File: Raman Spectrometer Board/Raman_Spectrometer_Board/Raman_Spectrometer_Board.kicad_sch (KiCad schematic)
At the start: 33 parts, among them J1 RJ45_LED_Shielded, Q1 BSS138, Q2 BSS138, Q3 BSS138, Q4 BSS138, SW1 SW_Push, SW2 SW_Push, U1 Teensy4.1_DEV-16771, U2 OKI 12V-5V

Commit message: Rev 2 updated
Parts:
- added Conn10, Conn9: Molex_SL_02, MRDT_Connectors:MOLEX_SL_02_Vertical, symbol MRDT_Connectors:Molex_SL_02
- Conn7: footprint (none) -> MRDT_Connectors:MOLEX_SL_04_Vertical
- Conn8: footprint (none) -> MRDT_Connectors:MOLEX_SL_02_Vertical
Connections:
- net +3V3 is gone; now on net +3.3V: Conn8.1
- net +3.3V: now also Conn10.1, Conn9.1
- net CCD_Vout: now also U1.34 (RX8); no longer U1.26 (A12)
- net Encoder A: now also U1.22 (A8); no longer U1.37 (CS3)
- net Encoder B: now also U1.23 (A9); no longer U1.36 (CS2)
- net Green_Laser_3.3V: now also U1.33 (MCLK2); no longer U1.23 (A9)
- net Limit Switch 1: now also U1.30 (CRX3)
- net SW1: now also U1.40 (A16); no longer U1.41 (A17)
- net SW2: now also U1.41 (A17); no longer U1.40 (A16)
- net Limit Switch 3: now reaches U1.28 (RX7)
- net Limit Switch 3: now also Conn10.2
- net Limit Switch 2: now reaches U1.29 (TX7)
- net Limit Switch 2: now also Conn9.2
- net Diode Control: no longer names the net of U1.2 (OUT2)
- net Green_LED: no longer names the net of U1.1 (TX1)
- net Red_LED: no longer names the net of U1.0 (RX1)
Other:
- note added: "Limit Switches"
- note added: "Motor Encoder"
- note removed: "Limit Switch"
- note removed: "Motor encoder"
- moved on the sheet: Conn8, U1

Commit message: updated Raman PCB
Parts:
- added Conn11: GimbalA, MRDT_Connectors:MOLEX_SL_03_Vertical, symbol MRDT_Connectors:Molex_SL_03
- added Conn12: GimbalB, MRDT_Connectors:MOLEX_SL_03_Vertical, symbol MRDT_Connectors:Molex_SL_03
- Conn10: value Molex_SL_02 -> LimitSwitch3
- Conn7: value Molex_SL_04 -> MotorEncoder
- Conn8: value Molex_SL_02 -> LimitSwitch1
- Conn9: value Molex_SL_02 -> LimitSwitch2
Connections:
- net +5V: now also Conn11.1, Conn12.1
- net GND: now also Conn11.3, Conn12.3
- net GimbalPWM_A: now reaches U1.36 (CS2)
- net GimbalPWM_A: now also Conn11.2
- net GimbalPWM_B: now reaches U1.37 (CS3)
- net GimbalPWM_B: now also Conn12.2
- no-connect marks 32 -> 30

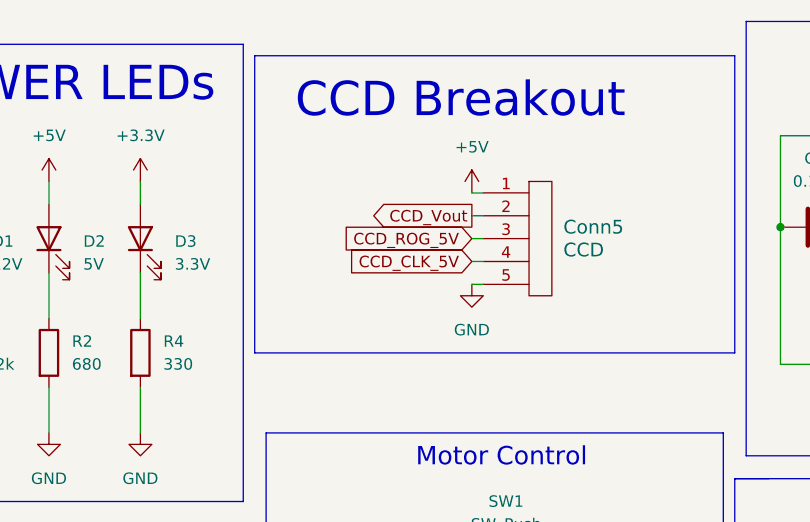
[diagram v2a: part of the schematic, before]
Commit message: Updated CCD SHSW as well as the pin connector between both boards. Still need to adjust an even frame size, adjust length of ethernet cables, generate GERBS, and check all input/output flags, as well as GND field. May have forgotten something
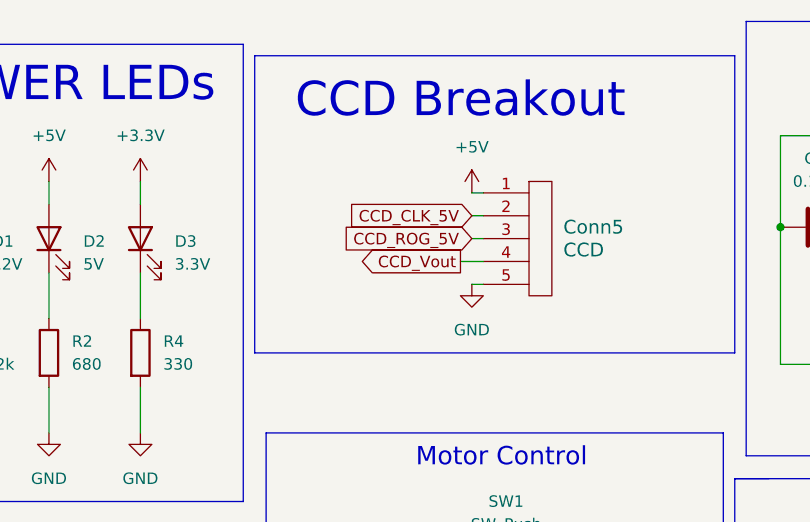
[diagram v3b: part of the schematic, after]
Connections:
- net CCD_CLK_5V: now also Conn5.2; no longer Conn5.4
- net CCD_Vout: now also Conn5.4; no longer Conn5.2

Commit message: Finished Rev2
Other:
- moved on the sheet: Conn11, Conn12

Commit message: Small touchups, Generated Gerbs
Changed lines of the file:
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@@
 			)
 		)
-		(property "Description" ""
+		(property "Description" "Power symbol creates a global label with name \"GND\" , ground"
 			(at 31.75 41.91 0)
 			(effects
@@
 			)
 		)
-		(property "Description" ""
+		(property "Description" "Unpolarized capacitor"
 			(at 209.55 39.37 0)
 			(effects
@@
 	)
 	(symbol
-		(lib_name "+12V_3")
 		(lib_id "power:+12V")
 		(at 135.89 114.3 0)
@@
 	)
 	(symbol
-		(lib_name "+12V_1")
 		(lib_id "power:+12V")
 		(at 114.3 34.29 0)
@@
 	)
 	(symbol
-		(lib_name "GND_4")
 		(lib_id "power:GND")
 		(at 177.8 133.35 0)
@@
 	)
 	(symbol
-		(lib_name "GND_1")
 		(lib_id "power:GND")
 		(at 124.46 62.23 0)
@@
 			)
 		)
-		(property "Description" ""
+		(property "Description" "RJ connector, 8P8C (8 positions 8 connected), two LEDs, Shielded"
 			(at 231.14 39.37 0)
 			(effects
@@
 	)
 	(symbol
-		(lib_name "GND_1")
 		(lib_id "power:GND")
 		(at 114.3 62.23 0)
@@
 	)
 	(symbol
-		(lib_name "GND_6")
 		(lib_id "power:GND")
 		(at 208.28 158.75 0)
@@
 			)
 		)
-		(property "Description" ""
+		(property "Description" "Power symbol creates a global label with name \"GND\" , ground"
 			(at 231.14 55.88 0)
 			(effects
@@
 			)
 		)
-		(property "Description" ""
+		(property "Description" "Power symbol creates a global label with name \"GND\" , ground"
 			(at 186.69 92.71 0)
 			(effects
@@
 	)
 	(symbol
-		(lib_name "GND_3")
 		(lib_id "power:GND")
 		(at 123.19 170.18 0)
@@
 	)
 	(symbol
-		(lib_name "+12V_2")
 		(lib_id "power:+12V")
 		(at 58.42 33.02 0)
@@
 	)
 	(symbol
-		(lib_name "GND_5")
 		(lib_id "power:GND")
 		(at 114.3 83.82 270)
@@
 	)
 	(symbol
-		(lib_name "GND_4")
 		(lib_id "power:GND")
 		(at 135.89 138.43 0)
@@
 			)
 		)
-		(property "Description" ""
+		(property "Description" "Power symbol creates a global label with name \"+12V\""
 			(at 33.02 29.21 0)
 			(effects
@@
 	(symbol
 		(lib_id "MRDT_Connectors:Molex_SL_06")
-		(at 128.27 97.79 0)
+		(at 125.73 95.25 0)
 		(unit 1)
 		(exclude_from_sim no)
@@
 		(on_board yes)
 		(dnp no)
-		(fields_autoplaced yes)
 		(property "Reference" "Conn2"
-			(at 129.54 86.3599 0)
+			(at 128.27 83.82 0)
 			(effects
 				(font
@@
 		)
 		(property "Value" "TOF Sensor"
-			(at 129.54 88.8999 0)
+			(at 128.27 86.36 0)
 			(effects
 				(font
@@
 		)
 		(property "Footprint" "MRDT_Connectors:MOLEX_SL_06_Vertical"
-			(at 128.27 97.79 0)
+			(at 125.73 95.25 0)
 			(effects
 				(font
@@
 		)
 		(property "Datasheet" ""
-			(at 128.27 97.79 0)
+			(at 125.73 95.25 0)
 			(effects
 				(font
@@
 		)
 		(property "Description" ""
-			(at 128.27 97.79 0)
+			(at 125.73 95.25 0)
 			(effects
 				(font
@@
 	)
 	(symbol
-		(lib_name "Molex_SL_05_1")
 		(lib_id "MRDT_Connectors:Molex_SL_05")
 		(at 218.44 139.7 0)
@@
 			)
 		)
-		(property "Description" ""
+		(property "Description" "Power symbol creates a global label with name \"GND\" , ground"
 			(at 82.55 167.64 0)
 			(effects
@@
 	)
 	(symbol
-		(lib_name "GND_6")
 		(lib_id "power:GND")
 		(at 166.37 158.75 0)
@@
 			)
 		)
-		(property "Description" ""
+		(property "Description" "Power symbol creates a global label with name \"GND\" , ground"
 			(at 186.69 77.47 0)
 			(effects
@@
 	)
 	(symbol
-		(lib_name "GND_1")
 		(lib_id "power:GND")
 		(at 134.62 62.23 0)
@@
 	)
 	(symbol
-		(lib_name "GND_2")
 		(lib_id "power:GND")
 		(at 72.39 46.99 0)
@@
 			)
 		)
-		(property "Description" ""
+		(property "Description" "Power symbol creates a global label with name \"GND\" , ground"
 			(at 171.45 45.72 0)
 			(effects
